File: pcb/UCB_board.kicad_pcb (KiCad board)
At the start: 4 copper layers, 160 x 100 mm, 154 parts, among them IC1 SN65HVD75DR, J1 DIN41612_02x32_AC, J2 TC2030, J3 Conn_01x02_Pin, T1 H1102NL, U1 W5500, U3 USBLC6-2SC6, U4 USBLC6-2SC6, U5 USBLC6-2SC6, U6 FM24C64B, U7 STM32H563VITx, Y1 3225-25M-SR, Y2 3225-25M-SR

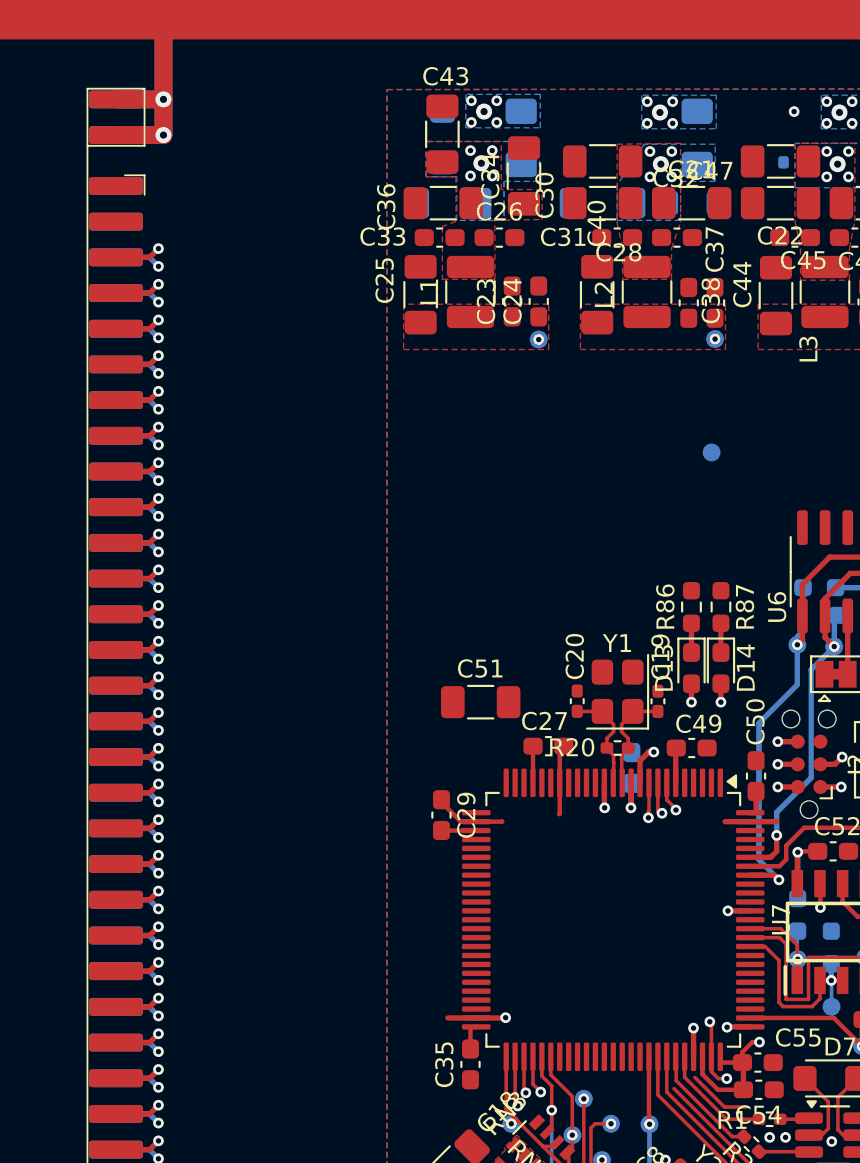
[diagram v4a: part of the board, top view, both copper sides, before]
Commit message: Add junction and bus entries to UniConnector schematic
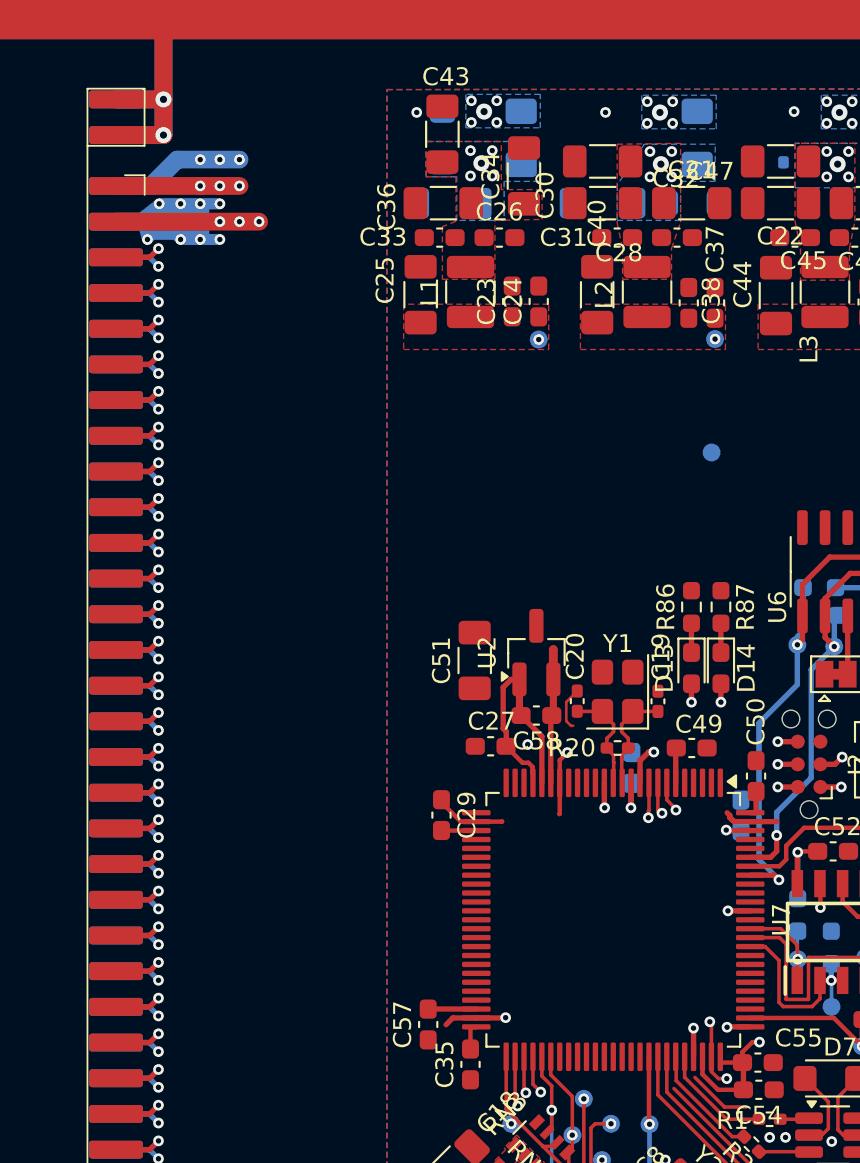
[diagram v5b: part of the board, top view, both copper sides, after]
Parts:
- added C56: 4,7u, Capacitor_SMD:C_0603_1608Metric_Pad1.08x0.95mm_HandSolder, B.Cu at (208.6, 96.3)
- added C57: 4,7u, Capacitor_SMD:C_0603_1608Metric_Pad1.08x0.95mm_HandSolder, F.Cu at (191.1, 108.0)
- added C58: 100n, Capacitor_SMD:C_0603_1608Metric_Pad1.08x0.95mm_HandSolder, F.Cu at (197.2, 90.7)
- added NT1: NetTie_2, NetTie:NetTie-2_SMD_Pad0.5mm, F.Cu at (198.1, 87.5)
- added U2: LM4040DBZ-3, Package_TO_SOT_SMD:SOT-23_Handsoldering, F.Cu at (197.2, 87.1)
- C29, C35, C49, C50, C53, C54, C55: value 10n -> 100n
- moved C27 3.24 mm to (194.6, 92.4), turned to 0 degrees
- moved C51 2.36 mm to (193.7, 87.6), turned to 90 degrees
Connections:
- net /MCU/SWO renamed /MCU/IO_20
- U7 pad 1: unconnected-(U7-PE2-Pad1) -> /MCU/IO_1
- U7 pad 15: unconnected-(U7-PC0-Pad15) -> /MCU/IO_7
- U7 pad 16: unconnected-(U7-PC1-Pad16) -> /MCU/IO_8
- U7 pad 17: unconnected-(U7-PC2-Pad17) -> /MCU/IO_9
- U7 pad 18: unconnected-(U7-PC3-Pad18) -> /MCU/IO_10
- U7 pad 2: unconnected-(U7-PE3-Pad2) -> /MCU/IO_2
- U7 pad 20: unconnected-(U7-VREF--Pad20) -> Net-(U2-A)
- U7 pad 21: unconnected-(U7-VREF+-Pad21) -> +3.3V
- U7 pad 23: unconnected-(U7-PA0-Pad23) -> /MCU/IO_11
- U7 pad 24: unconnected-(U7-PA1-Pad24) -> /MCU/IO_12
- U7 pad 25: unconnected-(U7-PA2-Pad25) -> /MCU/IO_13
- U7 pad 26: unconnected-(U7-PA3-Pad26) -> /MCU/IO_14
- U7 pad 3: unconnected-(U7-PE4-Pad3) -> /MCU/IO_3
- U7 pad 4: unconnected-(U7-PE5-Pad4) -> /MCU/IO_4
- U7 pad 48: unconnected-(U7-VCAP-Pad48) -> Net-(C57-Pad2)
- U7 pad 5: unconnected-(U7-PE6-Pad5) -> /MCU/IO_5
- U7 pad 7: unconnected-(U7-PC13-Pad7) -> /MCU/IO_6
- U7 pad 78: unconnected-(U7-PC10-Pad78) -> /MCU/IO_28
- U7 pad 79: unconnected-(U7-PC11-Pad79) -> /MCU/IO_27
- U7 pad 80: unconnected-(U7-PC12-Pad80) -> /MCU/IO_26
- U7 pad 81: unconnected-(U7-PD0-Pad81) -> /MCU/IO_25
- U7 pad 82: unconnected-(U7-PD1-Pad82) -> /MCU/IO_24
- U7 pad 83: unconnected-(U7-PD2-Pad83) -> /MCU/IO_23
- U7 pad 84: unconnected-(U7-PD3-Pad84) -> /MCU/IO_22
- U7 pad 88: unconnected-(U7-PD7-Pad88) -> /MCU/IO_21
- U7 pad 90: unconnected-(U7-PB4(NJTRST)-Pad90) -> /MCU/IO_19
- U7 pad 91: unconnected-(U7-PB5-Pad91) -> /MCU/IO_18
- U7 pad 92: unconnected-(U7-PB6-Pad92) -> /MCU/IO_17
- U7 pad 96: unconnected-(U7-PB9-Pad96) -> /MCU/IO_16
- U7 pad 97: unconnected-(U7-PE0-Pad97) -> /MCU/IO_15
- U7 pad 98: unconnected-(U7-VCAP-Pad98) -> Net-(C56-Pad2)
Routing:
- net +3.3V: track 68.1 -> 129.3 mm, vias 21 -> 24
- net +5V: track 9.11 -> 49.7 mm, vias 2 -> 5
- net +12V: track 0.00 -> 29.5 mm, vias 1 -> 4
- net GND: track 72.3 -> 82.6 mm, vias 19 -> 31
- net Net-(U2-A): track 0.00 -> 5.86 mm
- net Net-(C57-Pad2): track 0.00 -> 2.70 mm
- net Net-(C56-Pad2): track 0.00 -> 2.20 mm, vias 0 -> 1
- net unconnected-(U7-PC13-Pad7): track 1.74 -> 0.00 mm, vias 1 -> 0
- net /MCU/IO_6: track 0.00 -> 1.74 mm, vias 0 -> 1
- net /MCU/IO_20: track 12.5 -> 13.1 mm
